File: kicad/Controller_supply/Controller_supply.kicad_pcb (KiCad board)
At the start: 2 copper layers, 8 parts, among them J1 Conn_01x03_Pin, U1 MC7824, U2 MC7924

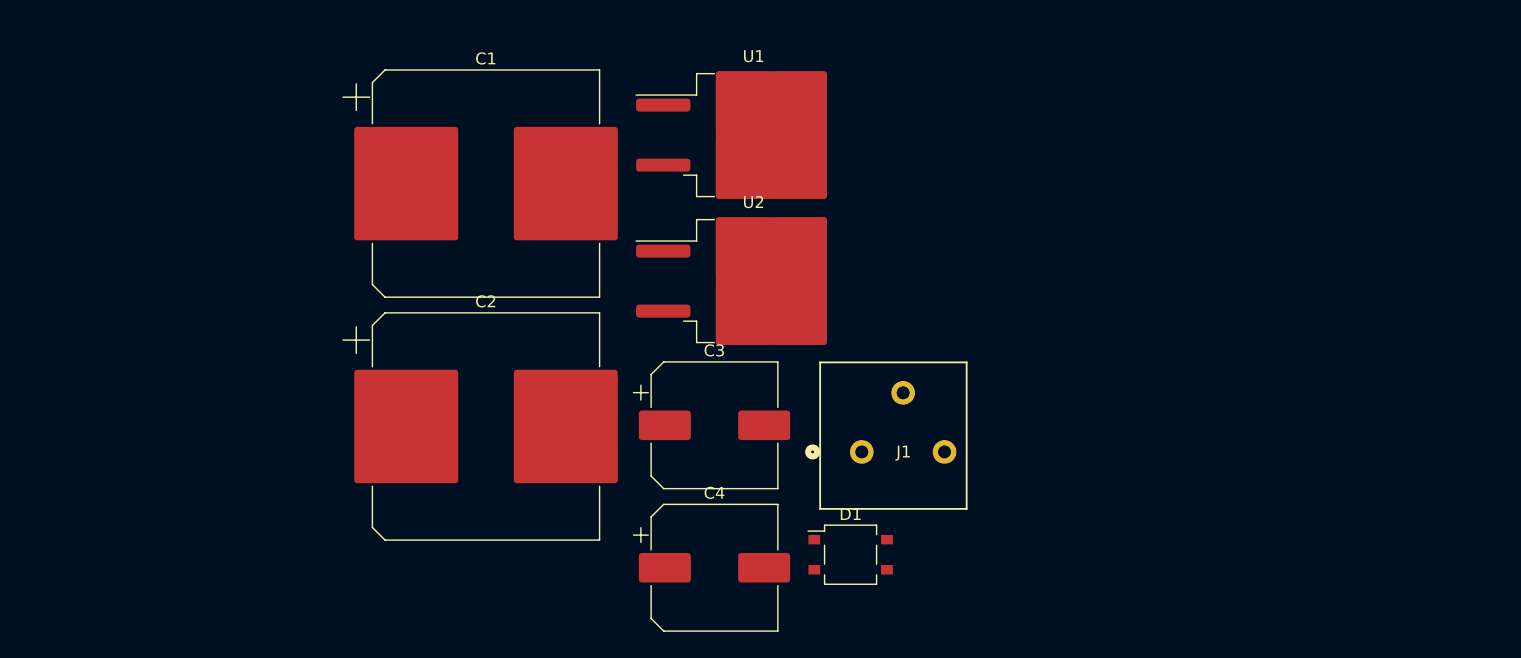
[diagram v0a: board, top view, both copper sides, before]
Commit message: 15V output modification
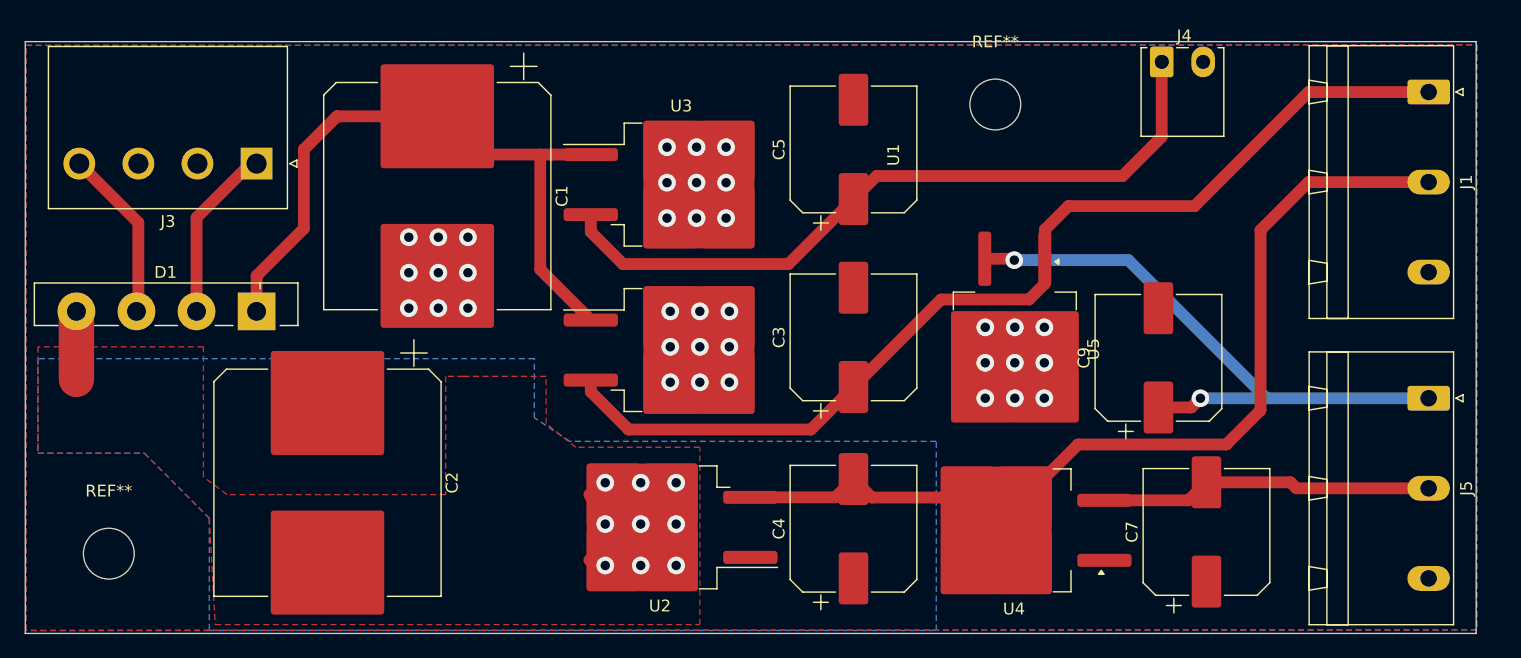
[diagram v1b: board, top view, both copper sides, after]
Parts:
- added C5: 220uF, Capacitor_SMD:CP_Elec_10x10.5, F.Cu at (152.0, 64.8)
- added C7: 220uF, Capacitor_SMD:CP_Elec_10x10.5, F.Cu at (181.9, 97.2)
- added C9: 220uF, Capacitor_SMD:CP_Elec_10x10.5, F.Cu at (177.8, 82.4)
- added J3: Conn_01x04_Pin, Connector_THT:Generic_pin-to-housing_1x04_P5.00mm_Horizontal, F.Cu at (101.5, 66.0)
- added J4: Conn_01x02, Connector_THT:Generic_7x7.5mm-footprt_1x02_P3.50mm_Horizontal, F.Cu at (178.1, 57.4)
- added J5: Conn_01x03_Pin, Connector_Phoenix_GMSTB:PhoenixContact_GMSTBA_2,5_3-G-7,62_1x03_P7.62mm_Horizontal, F.Cu at (200.7, 85.9)
- added REF**: MountingHole_4.3mm_M4, MountingHole:MountingHole_4.3mm_M4, F.Cu at (164.0, 61.0)
- added REF**: MountingHole_4.3mm_M4, MountingHole:MountingHole_4.3mm_M4, F.Cu at (89.0, 99.0)
- added U3: MC7824, Package_TO_SOT_SMD:TO-263-2, F.Cu at (137.4, 67.8)
- added U4: MC7915, Package_TO_SOT_SMD:TO-263-2, F.Cu at (165.6, 97.0)
- added U5: L7815, Package_TO_SOT_SMD:TO-263-2, F.Cu at (165.6, 81.7)
- D1: value CDBHD1100L-G -> GBU4A; footprint Package_TO_SOT_SMD:TO-269AA -> Diode_THT:Diode_Bridge_Vishay_GBU
- J1: footprint Connector_THT:CONN_1985205 -> Connector_Phoenix_GMSTB:PhoenixContact_GMSTBA_2,5_3-G-7,62_1x03_P7.62mm_Horizontal
- moved D1 54.3 mm to (101.5, 78.5), turned to 180 degrees
- moved J1 52.4 mm to (200.7, 59.9), turned to -90 degrees
- moved U2 22.3 mm to (135.6, 96.8), turned to 180 degrees
- moved U1 19.2 mm to (137.4, 81.8)
- moved C2 14.2 mm to (107.5, 93.0), turned to -90 degrees
- moved C3 13.9 mm to (152.0, 80.7), turned to 90 degrees
- moved C4 12.2 mm to (152.0, 96.9), turned to 90 degrees
- moved C1 4.25 mm to (116.8, 68.8), turned to -90 degrees
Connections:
- D1 pad 2: Net-(D1--) -> -24AC
- D1 pad 3: -24AC -> +24AC
- D1 pad 4: +24AC -> Net-(D1--)
- J1 pad 1: Line Hot -> +24VDC
- J1 pad 2: GND -> -24VDC
- J1 pad 3: Line Neutral -> GND
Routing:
- net +24VDC: track 0.00 -> 87.8 mm
- net -24VDC: track 0.00 -> 74.8 mm
- net +24VDC_fan: track 0.00 -> 61.7 mm
- net Net-(D1-+): track 0.00 -> 57.9 mm
- net +15VDC: track 0.00 -> 51.9 mm, vias 0 -> 2
- net -15VDC: track 0.00 -> 28.3 mm
- net Net-(D1--): track 0.00 -> 27.9 mm, vias 0 -> 9
- net -24AC: track 0.00 -> 14.9 mm
- net +24AC: track 0.00 -> 14.6 mm
- net GND: vias 0 -> 36
- added copper zone on B.Cu, net GND
- added copper zone on F.Cu, net GND
- added copper zone on B.Cu, net Net-(D1--)
- added copper zone on F.Cu, net Net-(D1--)
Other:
- board outline added: 122.8 x 50.1 mm

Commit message: Added silkscreen
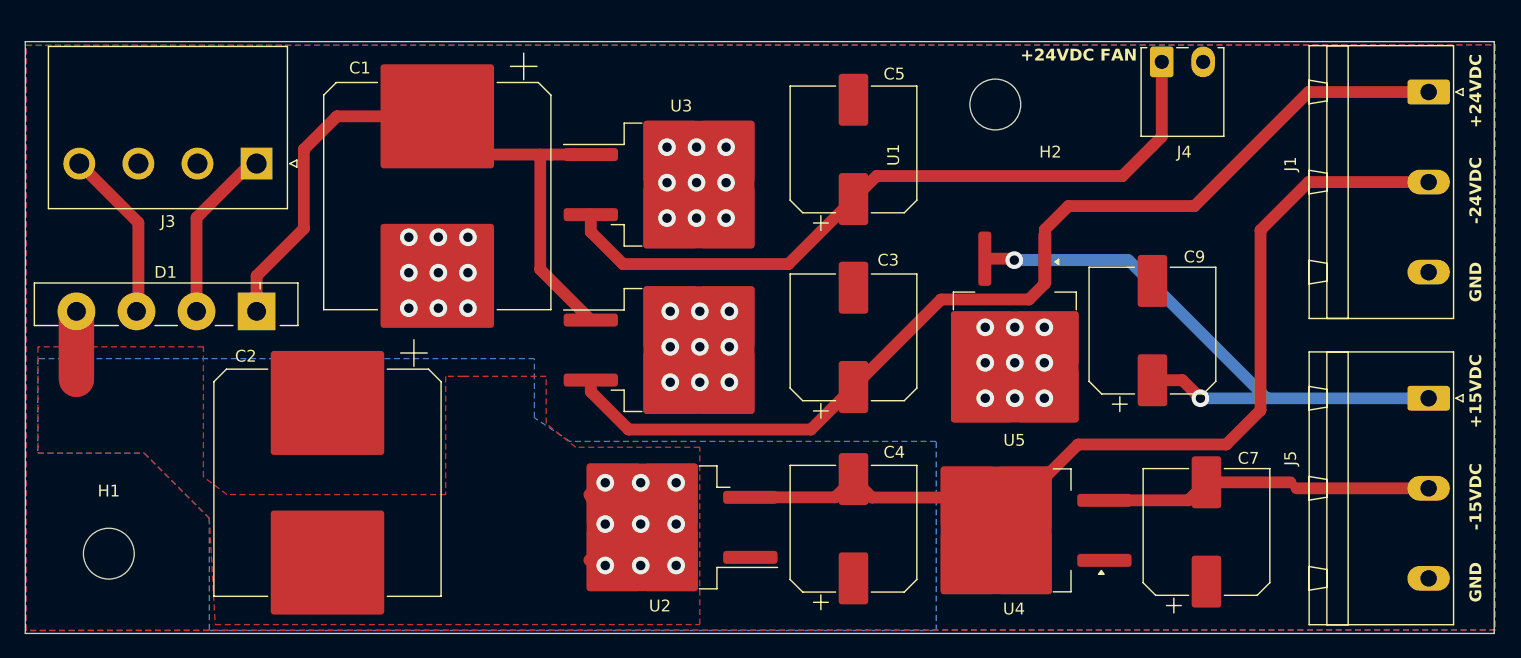
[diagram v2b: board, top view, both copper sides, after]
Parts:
- moved C9 2.36 mm to (177.3, 80.1)
- renumbered REF** to H1, REF** to H2
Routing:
- net +15VDC: track 51.9 -> 52.7 mm
- net -15VDC: track 28.3 -> 27.6 mm
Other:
- board size 122.8 x 50.1 mm -> 124.3 x 50.1 mm
- board text added: "+15VDC"
- board text added: "+24VDC"
- board text added: "+24VDC FAN"
- board text added: "-15VDC"
- board text added: "-24VDC"
- board text added: "GND"
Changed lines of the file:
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@@
 		(tags "D2PAK DDPAK TO-263 D2PAK-3 TO-263-3 SOT-404")
 		(property "Reference" "U5"
-			(at 0 -6.65 90)
+			(at 7.711 0.041122 0)
 			(layer "F.SilkS")
 			(effects
@@
 		(descr "Mounting Hole 4.3mm, no annular, M4")
 		(tags "mounting hole 4.3mm no annular m4")
-		(property "Reference" "REF**"
-			(at 0 -5.3 0)
+		(property "Reference" "H2"
+			(at 4.656 4.024 0)
 			(layer "F.SilkS")
 			(effects
@@
 		(tags "capacitor electrolytic")
 		(property "Reference" "C2"
-			(at 0 -10.55 90)
+			(at -10.704 6.916 180)
 			(layer "F.SilkS")
 			(effects
@@
 		(tags "connector Wago  top entry")
 		(property "Reference" "J4"
-			(at 1.9 -2.2 0)
+			(at 1.9 7.63 0)
 			(layer "F.SilkS")
 			(effects
@@
 		(tags "capacitor electrolytic")
 		(property "Reference" "C5"
-			(at 0 -6.3 90)
+			(at 6.38 3.448 180)
 			(layer "F.SilkS")
 			(effects
@@
 	(footprint "Capacitor_SMD:CP_Elec_10x10.5"
 		(layer "F.Cu")
-		(at 177.8 82.432 90)
+		(at 177.292 80.128 90)
 		(descr "SMD capacitor, aluminum electrolytic, Vishay 1010, 10.0x10.5mm, http://www.vishay.com/docs/28395/150crz.pdf")
 		(tags "capacitor electrolytic")
 		(property "Reference" "C9"
-			(at 0 -6.3 90)
+			(at 6.232 3.556 180)
 			(layer "F.SilkS")
 			(effects
@@
 		(tags "capacitor electrolytic")
 		(property "Reference" "C1"
-			(at 0 -10.55 90)
+			(at -10.838 6.554 180)
 			(layer "F.SilkS")
 			(effects
@@
 		(tags "capacitor electrolytic")
 		(property "Reference" "C4"
-			(at 0 -6.3 90)
+			(at 6.466 3.448 180)
 			(layer "F.SilkS")
 			(effects
@@
 		(descr "Mounting Hole 4.3mm, no annular, M4")
 		(tags "mounting hole 4.3mm no annular m4")
-		(property "Reference" "REF**"
+		(property "Reference" "H1"
 			(at 0 -5.3 0)
 			(layer "F.SilkS")
@@
 		(tags "capacitor electrolytic")
 		(property "Reference" "C7"
-			(at 0 -6.3 90)
+			(at 6.232 3.556 180)
 			(layer "F.SilkS")
 			(effects
@@
 		(tags "phoenix_contact connector GMSTBA_01x03_G_7.62mm")
 		(property "Reference" "J5"
-			(at 7.62 -3.2 90)
+			(at 5.08 11.684 90)
 			(layer "F.SilkS")
 			(effects
@@
 		(tags "phoenix_contact connector GMSTBA_01x03_G_7.62mm")
 		(property "Reference" "J1"
-			(at 7.62 -3.2 -90)
+			(at 6.096 11.684 -90)
 			(layer "F.SilkS")
 			(effects
@@
 		(tags "capacitor electrolytic")
 		(property "Reference" "C3"
-			(at 0 -6.3 90)
+			(at 6.532 2.94 180)
 			(layer "F.SilkS")
 			(effects
@@
 	(gr_rect
 		(start 81.93 55.68)
-		(end 204.68 105.75)
+		(end 206.204 105.75)
 		(stroke
 			(width 0.1)
@@
 		(layer "Edge.Cuts")
 	)
+	(gr_text "GND"
+		(at 205.232 77.724 90)
+		(layer "F.SilkS")
+		(effects
+			(font
+				(size 1 1)
+				(thickness 0.2)
+				(bold yes)
+			)
+			(justify left bottom)
+		)
+	)
+	(gr_text "+24VDC FAN"
+		(at 166.116 57.404 0)
+		(layer "F.SilkS")
+		(effects
+			(font
+				(size 1 1)
+				(thickness 0.2)
+				(bold yes)
+			)
+			(justify left bottom)
+		)
+	)
+	(gr_text "-15VDC"
+		(at 205.232 97.028 90)
+		(layer "F.SilkS")
+		(effects
+			(font
+				(size 1 1)
+				(thickness 0.2)
+				(bold yes)
+			)
+			(justify left bottom)
+		)
+	)
+	(gr_text "+24VDC"
+		(at 205.232 62.992 90)
+		(layer "F.SilkS")
+		(effects
+			(font
+				(size 1 1)
+				(thickness 0.2)
+				(bold yes)
+			)
+			(justify left bottom)
+		)
+	)
+	(gr_text "-24VDC"
+		(at 205.232 71.12 90)
+		(layer "F.SilkS")
+		(effects
+			(font
+				(size 1 1)
+				(thickness 0.2)
+				(bold yes)
+			)
+			(justify left bottom)
+		)
+	)
+	(gr_text "+15VDC"
+		(at 205.232 88.392 90)
+		(layer "F.SilkS")
+		(effects
+			(font
+				(size 1 1)
+				(thickness 0.2)
+				(bold yes)
+			)
+			(justify left bottom)
+		)
+	)
+	(gr_text "GND"
+		(at 205.232 103.124 90)
+		(layer "F.SilkS")
+		(effects
+			(font
+				(size 1 1)
+				(thickness 0.2)
+				(bold yes)
+			)
+			(justify left bottom)
+		)
+	)
 	(segment
 		(start 120.025 65.235)
@@
 	)
 	(segment
-		(start 188.976 92.964)
-		(end 189.484 93.472)
-		(width 1)
-		(layer "F.Cu")
-		(net 9)
-	)
-	(segment
 		(start 181.864 92.964)
 		(end 188.976 92.964)
@@
 	)
 	(segment
-		(start 177.8 86.632)
-		(end 180.576 86.632)
+		(start 165.487 74.047)
+		(end 165.608 74.168)
 		(width 1)
 		(layer "F.Cu")
@@
 	)
 	(segment
-		(start 165.487 74.047)
-		(end 165.608 74.168)
+		(start 179.832 84.328)
+		(end 181.356 85.852)
 		(width 1)
 		(layer "F.Cu")
@@
 	)
 	(segment
-		(start 180.576 86.632)
-		(end 181.356 85.852)
+		(start 177.292 84.328)
+		(end 179.832 84.328)
 		(width 1)
 		(layer "F.Cu")
@@
 		(polygon
 			(pts
-				(xy 82 56) (xy 204.736 55.949885) (xy 204.736 105.449885) (xy 82 105.5)
+				(xy 82 56) (xy 206.304 55.949885) (xy 206.304 105.449885) (xy 82 105.5)
 			)
 		)

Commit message: Seperated zones
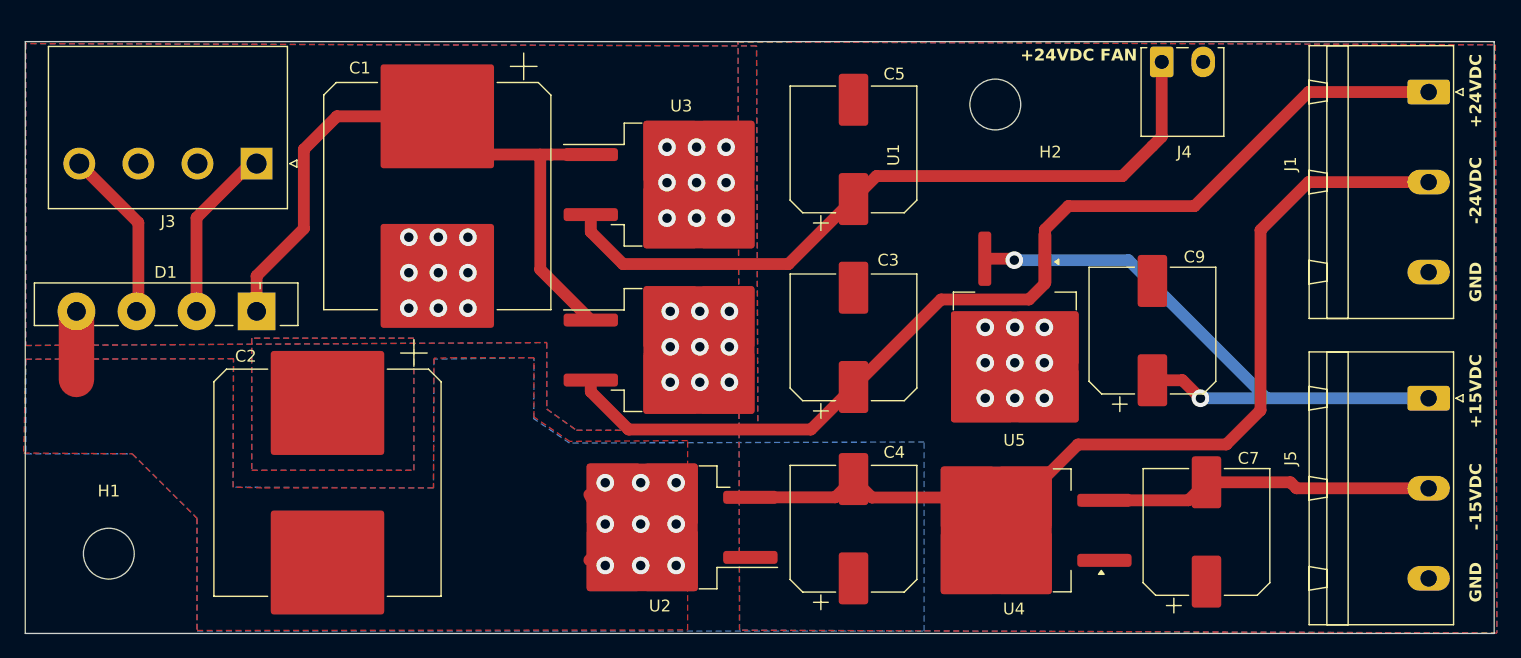
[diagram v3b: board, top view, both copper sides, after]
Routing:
- net -15VDC: track 27.6 -> 28.3 mm
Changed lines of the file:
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@@
+	)
+	(segment
+		(start 188.976 92.964)
+		(end 189.484 93.472)
+		(width 1)
+		(layer "F.Cu")
+		(net 9)
 	)
 	(segment
@@
 		(polygon
 			(pts
-				(xy 139 105) (xy 139 90) (xy 128.5 90) (xy 126 88) (xy 126 84) (xy 119 84) (xy 117.5 84) (xy 117.5 94)
-				(xy 103 94) (xy 99 94) (xy 97 92.5) (xy 97 81.5) (xy 83 81.5) (xy 83 90.5) (xy 92 90.5) (xy 97.5 96)
-				(xy 98 105)
+				(xy 137.968 105.453519) (xy 137.968 89.437519) (xy 128 89.5) (xy 124.968 87.437519) (xy 124.968 82.421519)
+				(xy 118.364 82.421519) (xy 116.509762 82.460205) (xy 116.468 93.437519) (xy 101.968 93.437519) (xy 99.510333 93.376466)
+				(xy 99.547169 82.5004) (xy 81.978986 82.5523) (xy 81.792852 90.485974) (xy 90.978986 90.5523) (xy 96.460597 96)
+				(xy 96.460597 105.5)
 			)
 		)
@@
 		(polygon
 			(pts
-				(xy 82 56) (xy 206.304 55.949885) (xy 206.304 105.449885) (xy 82 105.5)
+				(xy 142.232878 55.704) (xy 206.304 55.949885) (xy 206.43229 105.720377) (xy 142.361168 105.474492)
+			)
+		)
+	)
+	(zone
+		(net 2)
+		(net_name "GND")
+		(layers "F&B.Cu")
+		(hatch edge 0.5)
+		(priority 4)
+		(connect_pads
+			(clearance 1)
+		)
+		(min_thickness 0.25)
+		(filled_areas_thickness no)
+		(fill yes
+			(thermal_gap 0.5)
+			(thermal_bridge_width 0.5)
+		)
+		(polygon
+			(pts
+				(xy 101.092 80.772) (xy 101.092 91.948) (xy 114.808 91.948) (xy 114.808 80.772)
+			)
+		)
+	)
+	(zone
+		(net 2)
+		(net_name "GND")
+		(layers "F&B.Cu")
+		(hatch edge 0.5)
+		(priority 3)
+		(connect_pads
+			(clearance 1)
+		)
+		(min_thickness 0.25)
+		(filled_areas_thickness no)
+		(fill yes
+			(thermal_gap 0.5)
+			(thermal_bridge_width 0.5)
+		)
+		(polygon
+			(pts
+				(xy 81.964434 55.845668) (xy 81.964434 81.388668) (xy 126.051952 81.140953) (xy 126.047435 86.765848)
+				(xy 128.558434 88.557668) (xy 143.909434 88.606668) (xy 143.798434 56.045668)
 			)
 		)
@@
 		(polygon
 			(pts
-				(xy 159 89.5) (xy 128 89.5) (xy 125 87.5) (xy 125 82.5) (xy 83 82.5) (xy 83 90.5) (xy 92 90.5) (xy 97.5 96)
-				(xy 97.5 105.5) (xy 159 105.5)
+				(xy 157.978986 89.5523) (xy 127.978986 89.6443) (xy 124.946986 87.581819) (xy 124.968 82.421519)
+				(xy 116.501293 82.545304) (xy 116.468 93.437519) (xy 99.510333 93.376466) (xy 99.547169 82.5004)
+				(xy 81.978986 82.5523) (xy 81.978986 90.5523) (xy 90.978986 90.5523) (xy 96.460597 96) (xy 96.478986 105.5523)
+				(xy 157.978986 105.5523)
 			)
 		)
